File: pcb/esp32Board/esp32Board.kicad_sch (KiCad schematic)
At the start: 35 parts, among them J1 ESPProgJTAG_RX, J10 USB_C_Receptacle_USB2.0, J11 Conn_01x14_Female, J3 ESPProgUART_RX, J4 CAN, J5 UART2, J6 I2C, J7 InputOnly, J8 PWR, J9 GND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

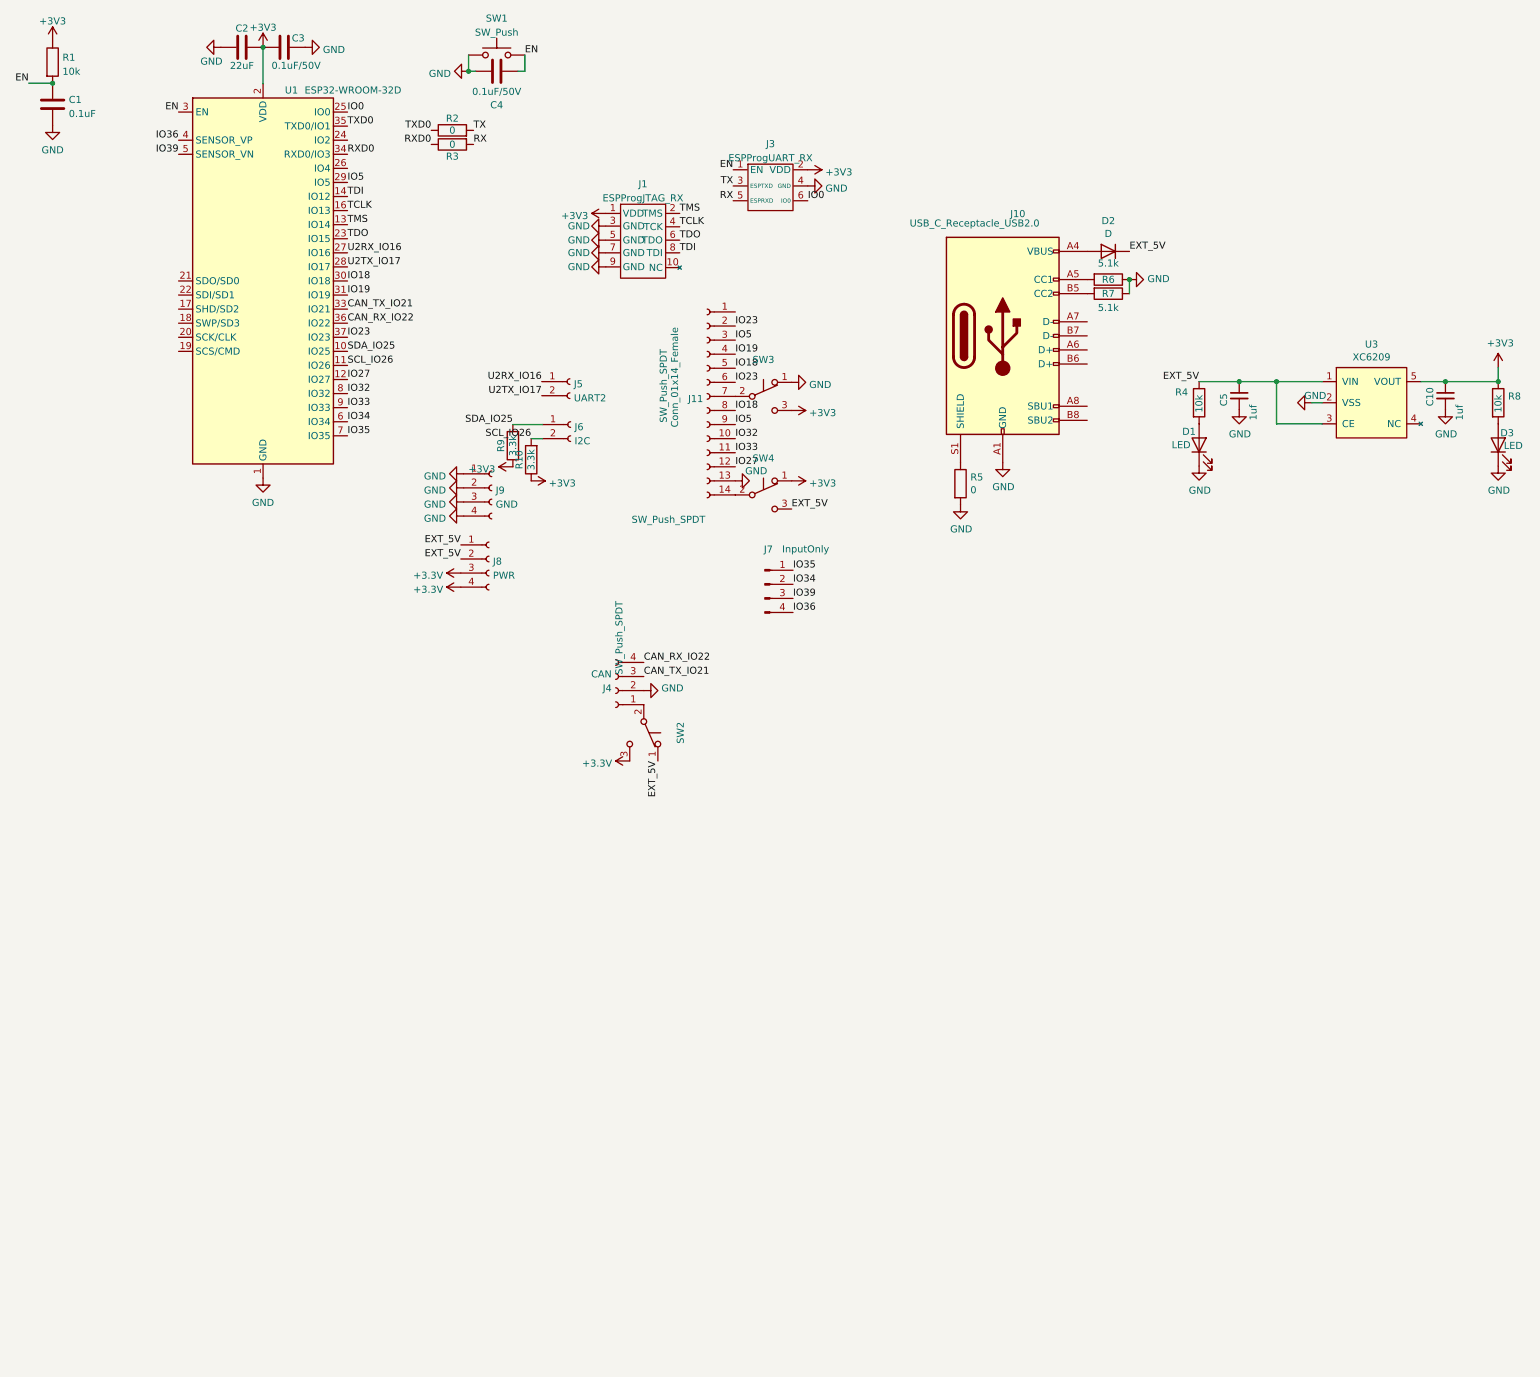
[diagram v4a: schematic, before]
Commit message: Update sch with blocks
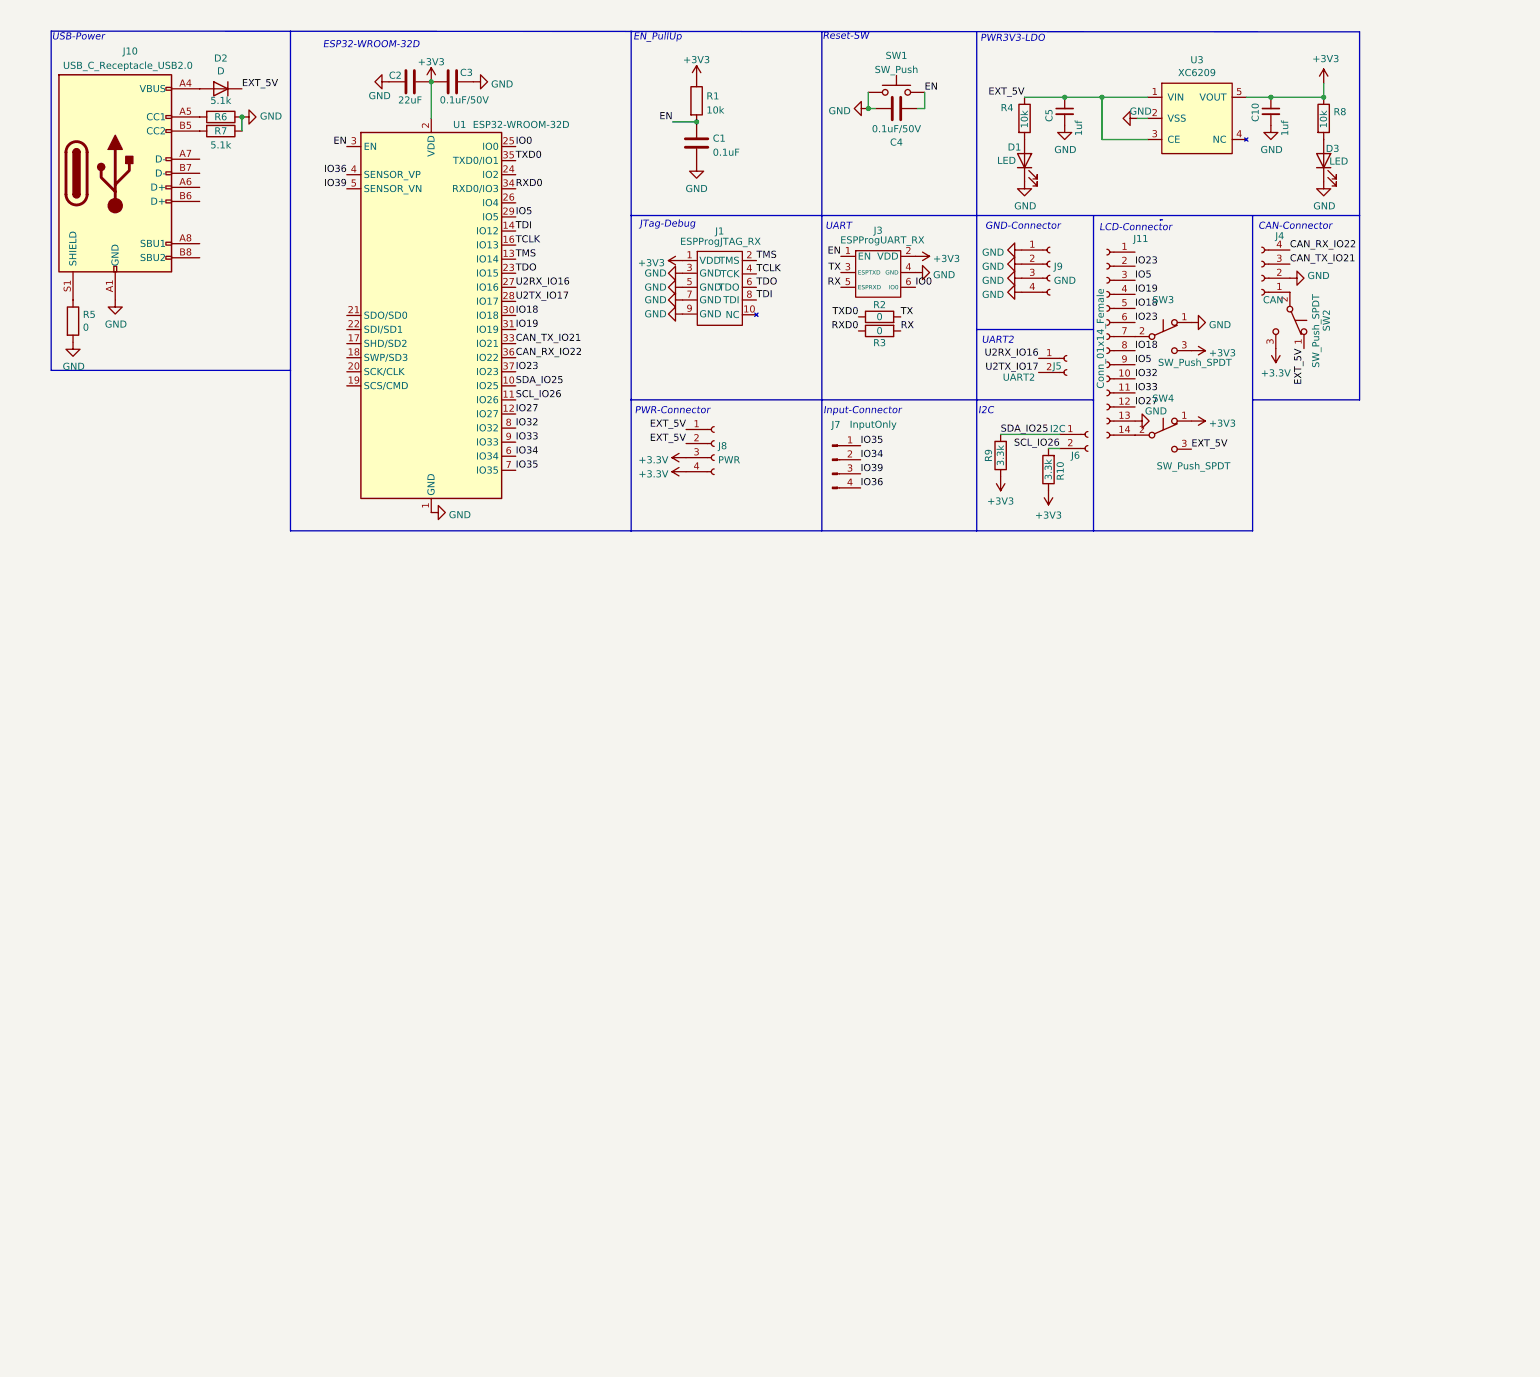
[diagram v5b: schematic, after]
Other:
- note added: "CAN-Connector"
- note added: "EN_PullUp"
- note added: "ESP32-WROOM-32D"
- note added: "GND-Connector"
- note added: "I2C"
- note added: "Input-Connector"
- note added: "JTag-Debug"
- note added: "LCD-Connector"
- note added: "PWR-Connector"
- note added: "PWR3V3-LDO"
- note added: "Reset-SW"
- note added: "UART"
- note added: "UART2"
- note added: "USB-Power"
- company: (none) -> 电子科技大学
- title: (none) -> 基于ESP32的物流节点控制单元设计
- moved on the sheet: C1, C10, C2, C3, C4, C5, D1, D2, D3, J1, J10, J11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

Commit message: 改成竖的，论文好看
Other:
- note added: "ESP32-WROOM-32D模块"
- note added: "JTag-调试"
- note added: "LCD-屏幕"
- note added: "USB电源输入"
- note added: "串口"
- note added: "复位上拉"
- note added: "复位开关"
- note added: "电源"
- note removed: "EN_PullUp"
- note removed: "ESP32-WROOM-32D"
- note removed: "JTag-Debug"
- note removed: "LCD-Connector"
- note removed: "PWR3V3-LDO"
- note removed: "Reset-SW"
- note removed: "UART"
- note removed: "USB-Power"
- moved on the sheet: C1, C10, C2, C3, C4, C5, D1, D2, D3, J1, J10, J11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
